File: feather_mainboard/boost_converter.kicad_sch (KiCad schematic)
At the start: 6 parts, among them U1 WPME-FISM_SMT-8

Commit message: schematic is almost done (check TODOs in schematic file)
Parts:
- renumbered C4 to C3, C3 to C4, C2 to C5, C1 to C6, U1 to U4
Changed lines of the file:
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@@
 		(on_board yes)
 		(dnp no)
-		(property "Reference" "U1"
+		(property "Reference" "U4"
 			(at 147.32 91.948 0)
 			(effects
@@
 			(project "feather_mainboard"
 				(path "/e1e12730-ab4f-45db-8b66-c1e0f78e2f00/bcd38403-f30d-4d25-9221-d4e2b9310dad"
-					(reference "U1")
+					(reference "U4")
 					(unit 1)
 				)
@@
 		(on_board yes)
 		(dnp no)
-		(property "Reference" "C2"
+		(property "Reference" "C5"
 			(at 124.968 99.06 90)
 			(effects
@@
 			(project "feather_mainboard"
 				(path "/e1e12730-ab4f-45db-8b66-c1e0f78e2f00/bcd38403-f30d-4d25-9221-d4e2b9310dad"
-					(reference "C2")
+					(reference "C5")
 					(unit 1)
 				)
@@
 		(on_board yes)
 		(dnp no)
-		(property "Reference" "C1"
+		(property "Reference" "C6"
 			(at 105.41 99.06 90)
 			(effects
@@
 			(project "feather_mainboard"
 				(path "/e1e12730-ab4f-45db-8b66-c1e0f78e2f00/bcd38403-f30d-4d25-9221-d4e2b9310dad"
-					(reference "C1")
+					(reference "C6")
 					(unit 1)
 				)
@@
 		(on_board yes)
 		(dnp no)
-		(property "Reference" "C4"
+		(property "Reference" "C3"
 			(at 165.354 99.568 90)
 			(effects
@@
 			(project "feather_mainboard"
 				(path "/e1e12730-ab4f-45db-8b66-c1e0f78e2f00/bcd38403-f30d-4d25-9221-d4e2b9310dad"
-					(reference "C4")
+					(reference "C3")
 					(unit 1)
 				)
@@
 		(on_board yes)
 		(dnp no)
-		(property "Reference" "C3"
+		(property "Reference" "C4"
 			(at 147.32 81.534 0)
 			(effects
@@
 			(project "feather_mainboard"
 				(path "/e1e12730-ab4f-45db-8b66-c1e0f78e2f00/bcd38403-f30d-4d25-9221-d4e2b9310dad"
-					(reference "C3")
-					(unit 1)
-				)
+					(reference "C4")
+					(unit 1)
+				)

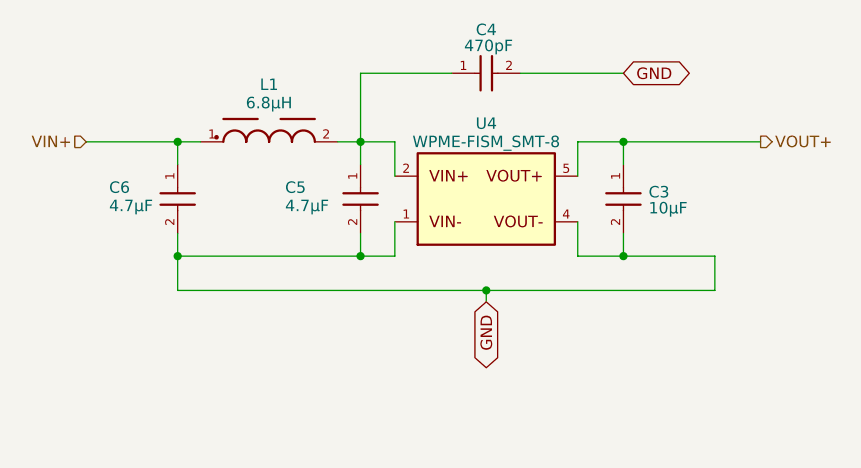
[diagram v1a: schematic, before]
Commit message: changed footprints location to match the new folder. TODO: check if the path is working on another computer
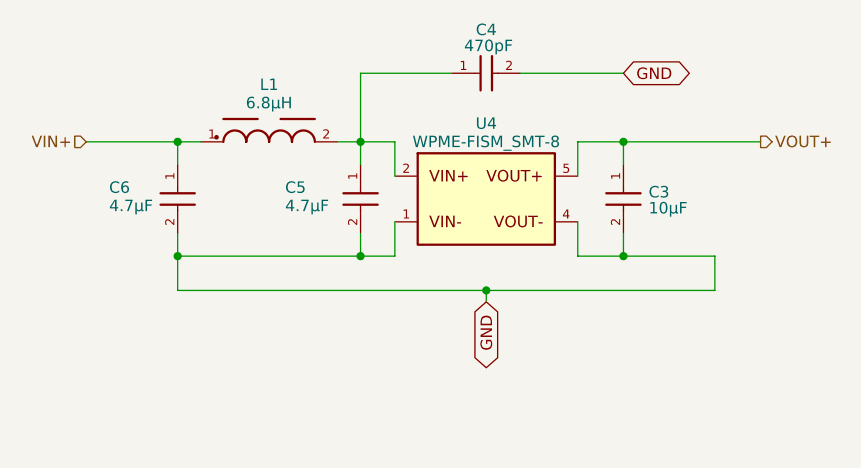
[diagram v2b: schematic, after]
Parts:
- C3, C5, C6: footprint footprints:WCAP-CSGP_1210_H2.0 -> Custom footprints:WCAP-CSGP_1210_H2.0
- C4: footprint footprints:WCAP-CSMH_1808_H2.0 -> Custom footprints:WCAP-CSMH_1808_H2.0
- L1: footprint footprints:WE-PD2_4532 -> Custom footprints:WE-PD2_4532
- U4: footprint footprints:WPME-FISM_SMT-8_L13.2W11.4H7.25 -> Custom footprints:WPME-FISM_SMT-8_L13.2W11.4H7.25
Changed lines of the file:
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@@
 			)
 		)
-		(property "Footprint" "footprints:WPME-FISM_SMT-8_L13.2W11.4H7.25"
+		(property "Footprint" "Custom footprints:WPME-FISM_SMT-8_L13.2W11.4H7.25"
 			(at 147.32 100.33 0)
 			(effects
@@
 	)
 	(symbol
+		(lib_name "WCAP-CSGP_1210_H2.0_2")
 		(lib_id "WCAP-CSGP_1210_H2.0:WCAP-CSGP_1210_H2.0")
 		(at 133.35 99.06 270)
@@
 			)
 		)
-		(property "Footprint" "footprints:WCAP-CSGP_1210_H2.0"
+		(property "Footprint" "Custom footprints:WCAP-CSGP_1210_H2.0"
 			(at 133.35 99.06 0)
 			(effects
@@
 			)
 		)
-		(property "Footprint" "footprints:WCAP-CSGP_1210_H2.0"
+		(property "Footprint" "Custom footprints:WCAP-CSGP_1210_H2.0"
 			(at 113.03 99.06 0)
 			(effects
@@
 	)
 	(symbol
+		(lib_name "WCAP-CSGP_1210_H2.0_1")
 		(lib_id "WCAP-CSGP_1210_H2.0:WCAP-CSGP_1210_H2.0")
 		(at 162.56 99.06 270)
@@
 			)
 		)
-		(property "Footprint" "footprints:WCAP-CSGP_1210_H2.0"
+		(property "Footprint" "Custom footprints:WCAP-CSGP_1210_H2.0"
 			(at 162.56 99.06 0)
 			(effects
@@
 			)
 		)
-		(property "Footprint" "footprints:WCAP-CSMH_1808_H2.0"
+		(property "Footprint" "Custom footprints:WCAP-CSMH_1808_H2.0"
 			(at 146.05 86.36 0)
 			(effects
@@
 			)
 		)
-		(property "Footprint" "footprints:WE-PD2_4532"
+		(property "Footprint" "Custom footprints:WE-PD2_4532"
 			(at 123.19 93.98 0)
 			(effects

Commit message: added daughter board
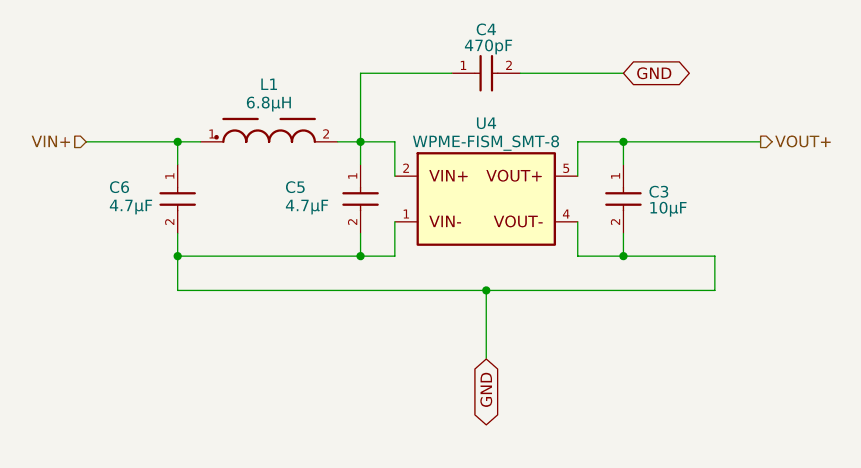
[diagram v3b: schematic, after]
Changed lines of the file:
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@@
 	(wire
 		(pts
-			(xy 147.32 110.49) (xy 147.32 111.76)
+			(xy 147.32 110.49) (xy 147.32 118.11)
 		)
 		(stroke
@@
 	(global_label "GND"
 		(shape bidirectional)
-		(at 147.32 111.76 270)
+		(at 147.32 118.11 270)
 		(fields_autoplaced yes)
 		(effects
@@
 		)
 		(property "Intersheetrefs" "${INTERSHEET_REFS}"
-			(at 147.32 119.727 90)
+			(at 147.32 126.077 90)
 			(effects
 				(font

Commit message: finished mainboard design, need to do the routing
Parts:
- renumbered C3 to C2_1, C4 to C3, C5 to C4_1, C6 to C4_2
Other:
- moved on the sheet: C2_1, C3
